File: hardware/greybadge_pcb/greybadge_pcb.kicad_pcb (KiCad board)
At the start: 2 copper layers, 75 x 99 mm, 148 parts, among them J1 Conn_02x05_Row_Letter_First, J2 Conn_02x05_Row_Letter_First, J3 Conn_02x05_Row_Letter_First, J4 Conn_02x05_Row_Letter_First, J5 USB_C_Receptacle_USB2.0, Q1 Q_NMOS_GSD, SW1 SW_Push, SW2 SW_Push, SW3 SW_Push, SW4 SW_Push, SW5 SW_Push, SW6 SW_Push, SW7 SW_Push, SW8 SW_Push, SW9 SW_Push, U1 TLV62568DBV, U2 TLV62568DBV, U3 TLV73325PDBV, U4 W25Q128JVS, U5 RP2350_60QFN, U7 ECP5U_25_CABGA256, U8 W25Q128JVSIM, X1 SiT2001B, Y1 12Mhz

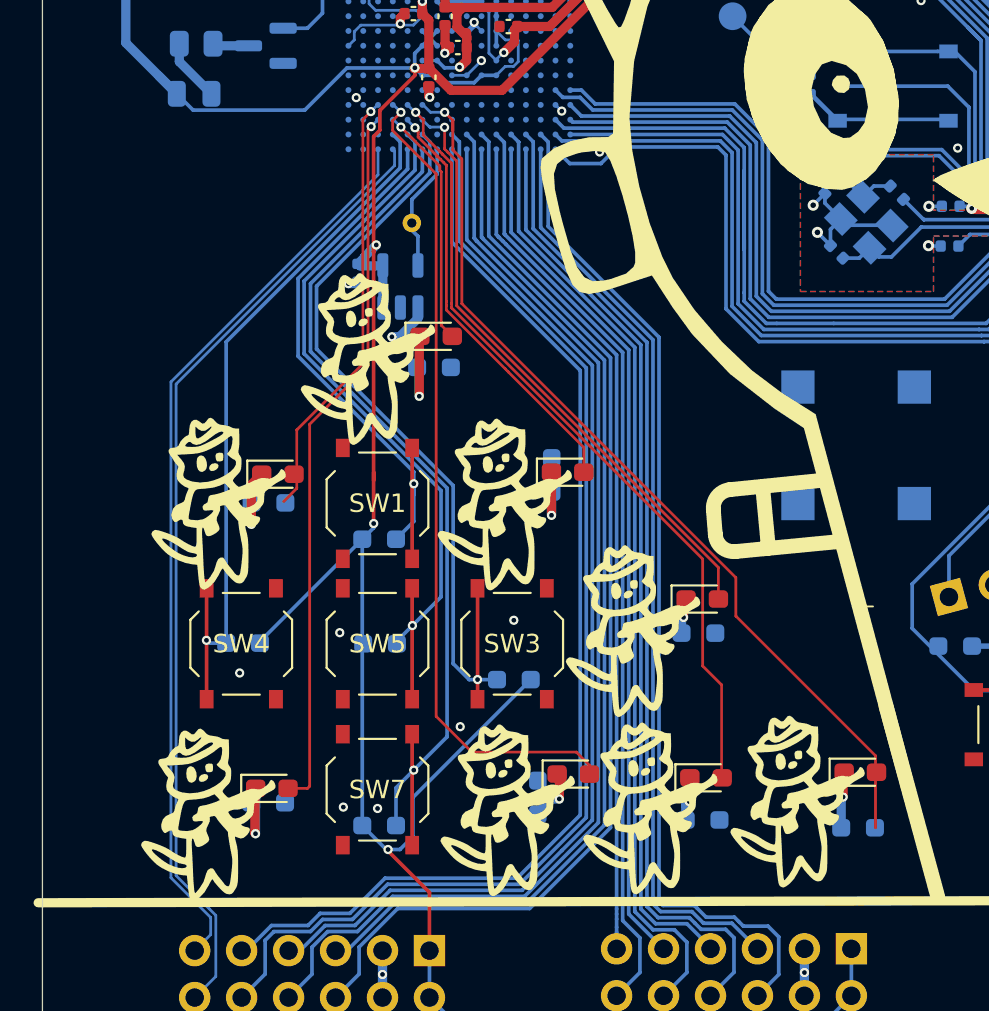
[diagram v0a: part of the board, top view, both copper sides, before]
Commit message: feat: nsf section
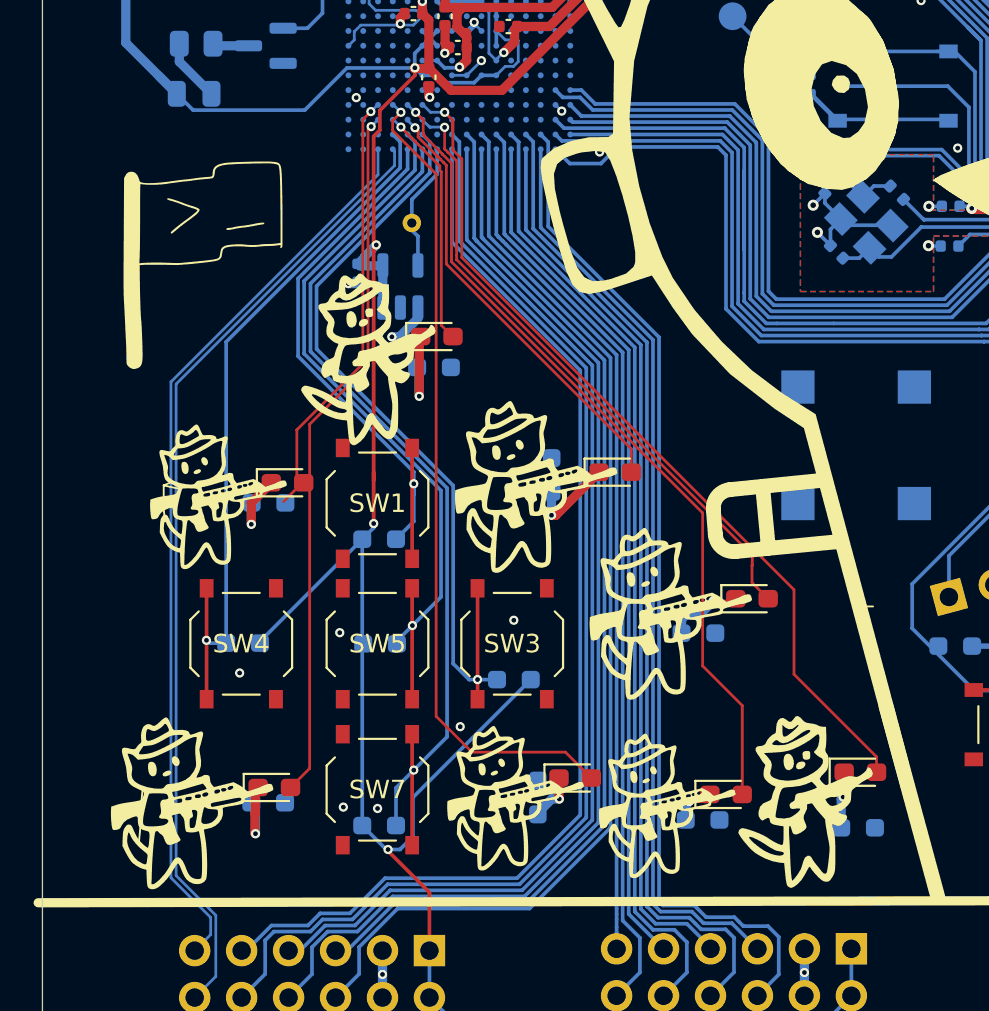
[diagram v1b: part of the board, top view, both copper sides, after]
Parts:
- removed the G*** at (107.2, 129.8)
- removed the G*** at (122.9, 129.3)
- removed the G*** at (99.7, 105.4)
- removed the G*** at (91.0, 130.0)
- removed the G*** at (91.6, 113.2)
- removed the G*** at (107.1, 113.2)
- added G***: LOGO, LOGO, F.Cu at (89.9, 129.3)
- added G***: LOGO, LOGO, F.Cu at (108.5, 112.2)
- added G***: LOGO, LOGO, F.Cu at (107.4, 129.0)
- added G***: LOGO, LOGO, F.Cu at (115.8, 119.0)
- added G***: LOGO, LOGO, F.Cu at (91.3, 112.7)
- added G***: LOGO, LOGO, F.Cu at (90.5, 100.2)
- added G***: LOGO, LOGO, F.Cu at (115.6, 129.4)
- moved G*** 20.5 mm to (99.7, 105.4)
- moved G*** 8.40 mm to (123.3, 129.3)
- moved D6 2.69 mm to (120.1, 118.3)
- moved D2 2.58 mm to (112.7, 111.4)
- moved D4 1.41 mm to (118.7, 128.9)
- moved D3 0.70 mm to (95.0, 112.0)
- moved D8 0.24 mm to (110.6, 128.0)
- moved D1 0.14 mm to (94.3, 128.5)
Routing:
- net D6: track 50.3 -> 47.3 mm
- net Net-(D6-K): track 1.94 -> 4.14 mm
- net D5: track 43.5 -> 44.8 mm
- net Net-(D2-K): track 3.60 -> 4.81 mm
- net C6: track 33.0 -> 34.1 mm
- net C5: track 23.0 -> 24.1 mm
- net C3: track 38.9 -> 38.3 mm
- net D4: track 44.8 -> 44.2 mm

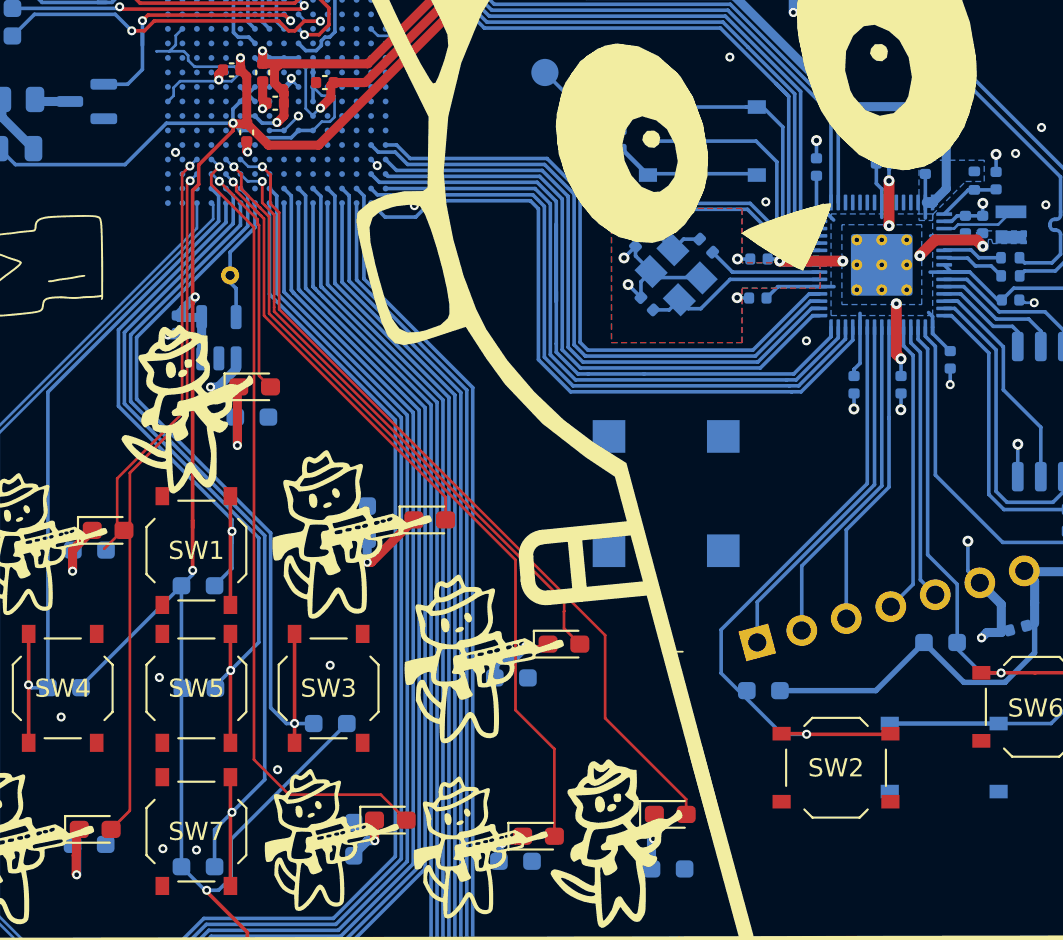
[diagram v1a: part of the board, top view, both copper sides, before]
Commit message: feat: oled move to top sch
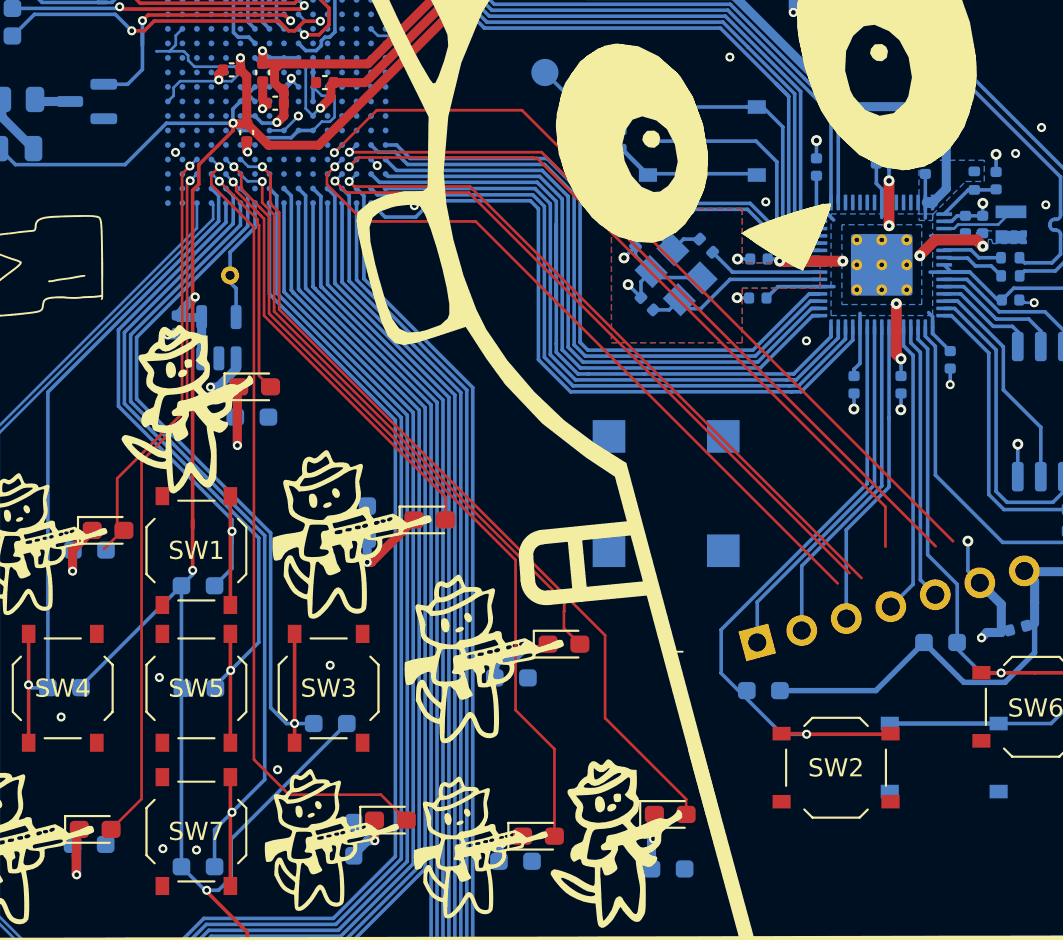
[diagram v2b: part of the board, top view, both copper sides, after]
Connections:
- net /rp2350/OLED_CS renamed OLED_CS
- net /rp2350/OLED_DC renamed OLED_DC
- net /rp2350/OLED_RST renamed OLED_RST
- net /rp2350/OLED_SCL renamed OLED_SCL
- net /rp2350/OLED_SDA renamed OLED_SDA
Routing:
- net E13: track 0.02 -> 45.5 mm, vias 0 -> 1
- net E14: track 0.02 -> 41.9 mm, vias 0 -> 1
- net D14: track 0.04 -> 40.6 mm, vias 0 -> 1
- net D13: track 0.01 -> 39.0 mm, vias 0 -> 1
- net C14: track 0.00 -> 37.9 mm, vias 0 -> 1
- net C13: track 0.01 -> 37.9 mm, vias 0 -> 1

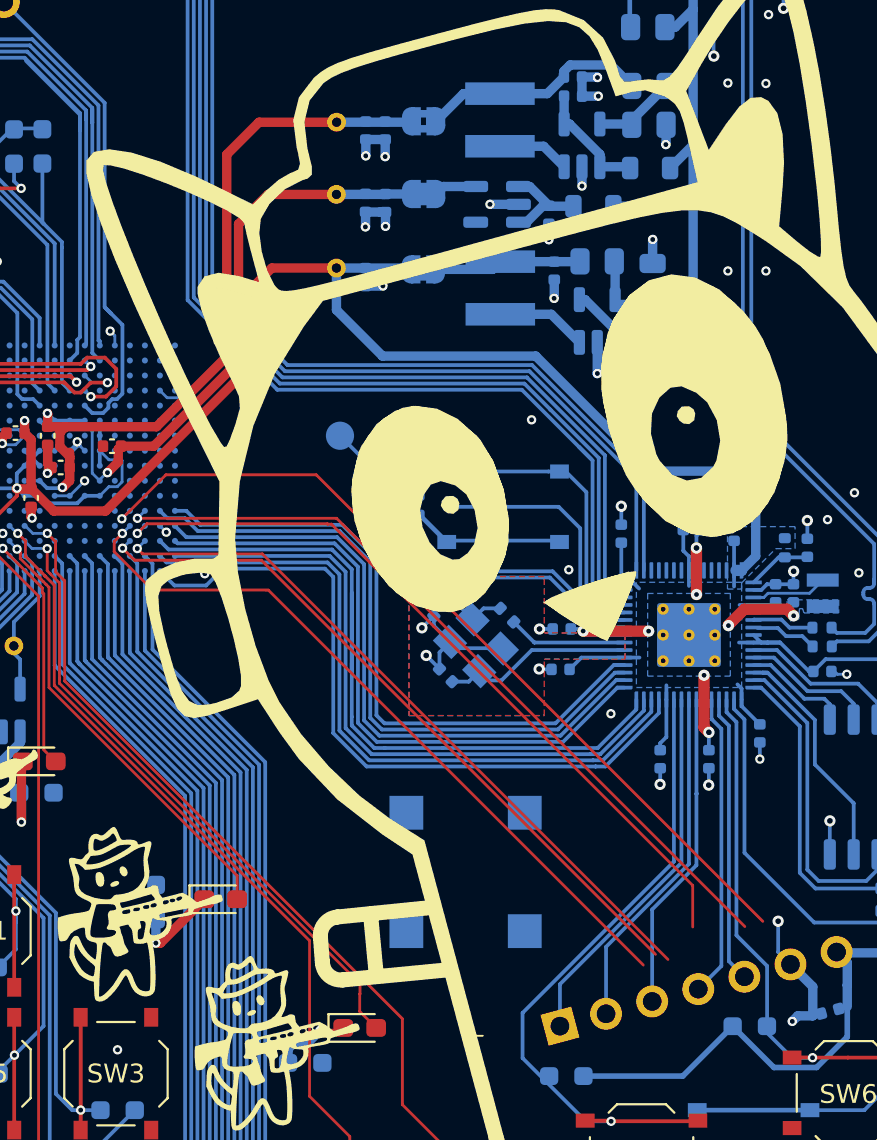
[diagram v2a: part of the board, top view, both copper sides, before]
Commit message: feat: oled to fpga
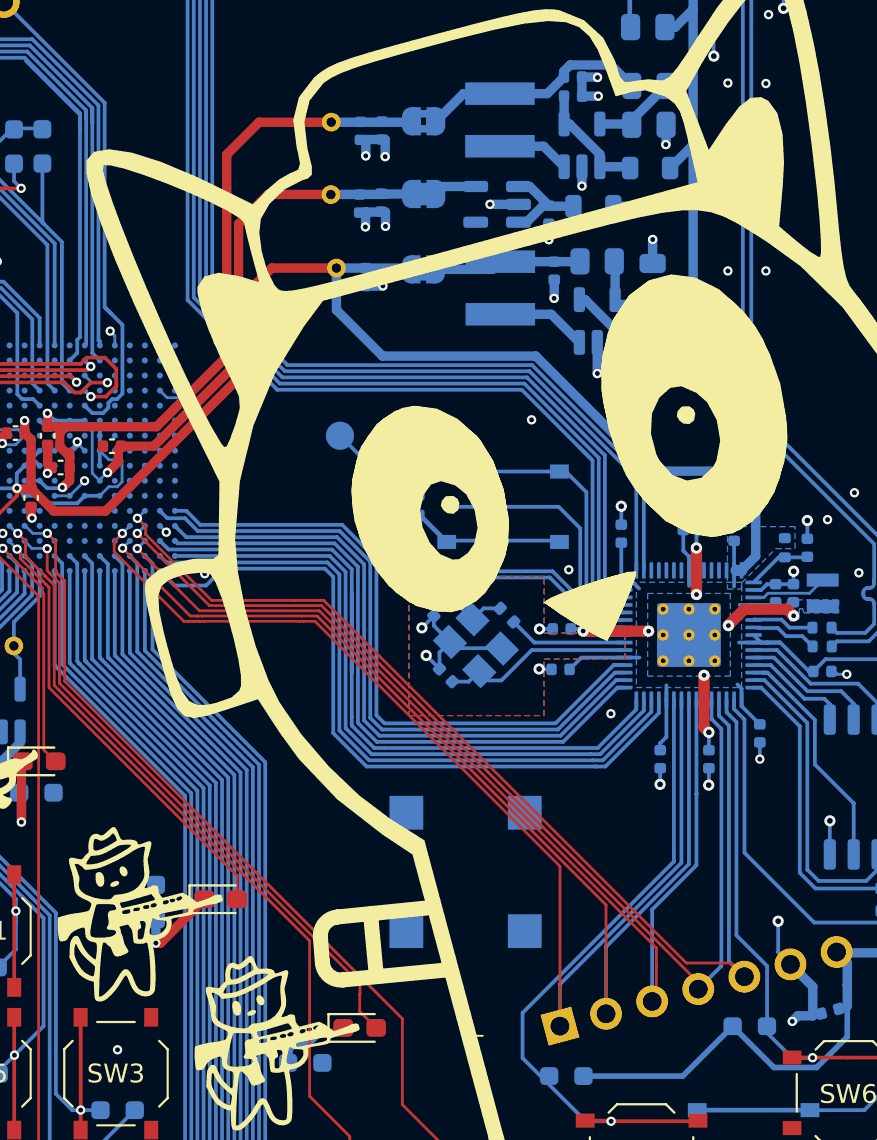
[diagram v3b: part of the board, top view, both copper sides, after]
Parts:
- moved C16 0.32 mm to (120.1, 74.4)
- moved TP3 0.30 mm to (118.6, 73.9)
- moved C5 0.29 mm to (120.2, 70.5)
- moved TP1 0.29 mm to (118.6, 70.1)
- moved C14 0.24 mm to (121.3, 74.4)
- moved C8 0.17 mm to (121.3, 70.5)
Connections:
- GC9A1 pad 1: OLED_RST -> D13
- GC9A1 pad 2: OLED_CS -> C13
- GC9A1 pad 3: OLED_DC -> C14
- GC9A1 pad 4: OLED_SDA -> D14
- GC9A1 pad 5: OLED_SCL -> E14
- U5 pad 4: OLED_SCL -> E14
- U5 pad 5: OLED_SDA -> D14
- U5 pad 7: OLED_DC -> C14
- U5 pad 8: OLED_CS -> C13
- U5 pad 9: OLED_RST -> D13
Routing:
- net E13: track 45.5 -> 0.02 mm, vias 1 -> 0
- net D13: track 39.0 -> 61.0 mm
- net C13: track 37.9 -> 58.5 mm
- net OLED_RST: track 20.1 -> 0.00 mm
- net C14: track 37.9 -> 57.4 mm
- net OLED_CS: track 18.5 -> 0.00 mm
- net OLED_DC: track 17.4 -> 0.00 mm
- net E14: track 41.9 -> 58.6 mm
- net D14: track 40.6 -> 56.9 mm
- net OLED_SDA: track 16.1 -> 0.00 mm
- net OLED_SCL: track 15.3 -> 0.00 mm

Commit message: feat: artwork positioning i think
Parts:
- moved G*** 2.15 mm to (117.2, 111.7)
- moved G*** 1.05 mm to (107.5, 114.9)
- moved G*** 0.79 mm to (97.1, 118.4)
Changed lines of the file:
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@@
 	(footprint "LOGO"
 		(layer "B.Cu")
-		(at 106.761891 115.740564 180)
+		(at 107.455841 114.948711 180)
 		(property "Reference" "G***"
 			(at 0 -0.024412 0)
@@
 	(footprint "LOGO"
 		(layer "B.Cu")
-		(at 116.511001 113.747652 180)
+		(at 117.24994 111.725587 180)
 		(property "Reference" "G***"
 			(at 0 -0.024412 0)
@@
 	(footprint "LOGO"
 		(layer "B.Cu")
-		(at 97.766856 118.056651 180)
+		(at 97.051696 118.39412 180)
 		(property "Reference" "G***"
 			(at 0 0.14 0)
